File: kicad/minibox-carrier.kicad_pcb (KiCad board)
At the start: 2 copper layers, 109 x 101 mm, 9 parts, among them J1 ESP32-S3 LEFT - USB AT BOTTOM, J10 LCD VCC - WIRE AFTER VOLTAGE 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, J2 ESP32-S3 RIGHT - USB AT BOTTOM, J3 INMP441 VDD GND SCK WS SD L/R, J4 MAX98357A LRC BCLK DIN GAIN S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, J5 PCF8563T CLK INT SDA SCL VCC 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, J6 ST7796 PROVISIONAL HEADER, J7 SWITCH IN LOAD GND - VERIFY O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, J8 EXTERNAL 5V INPUT + GND

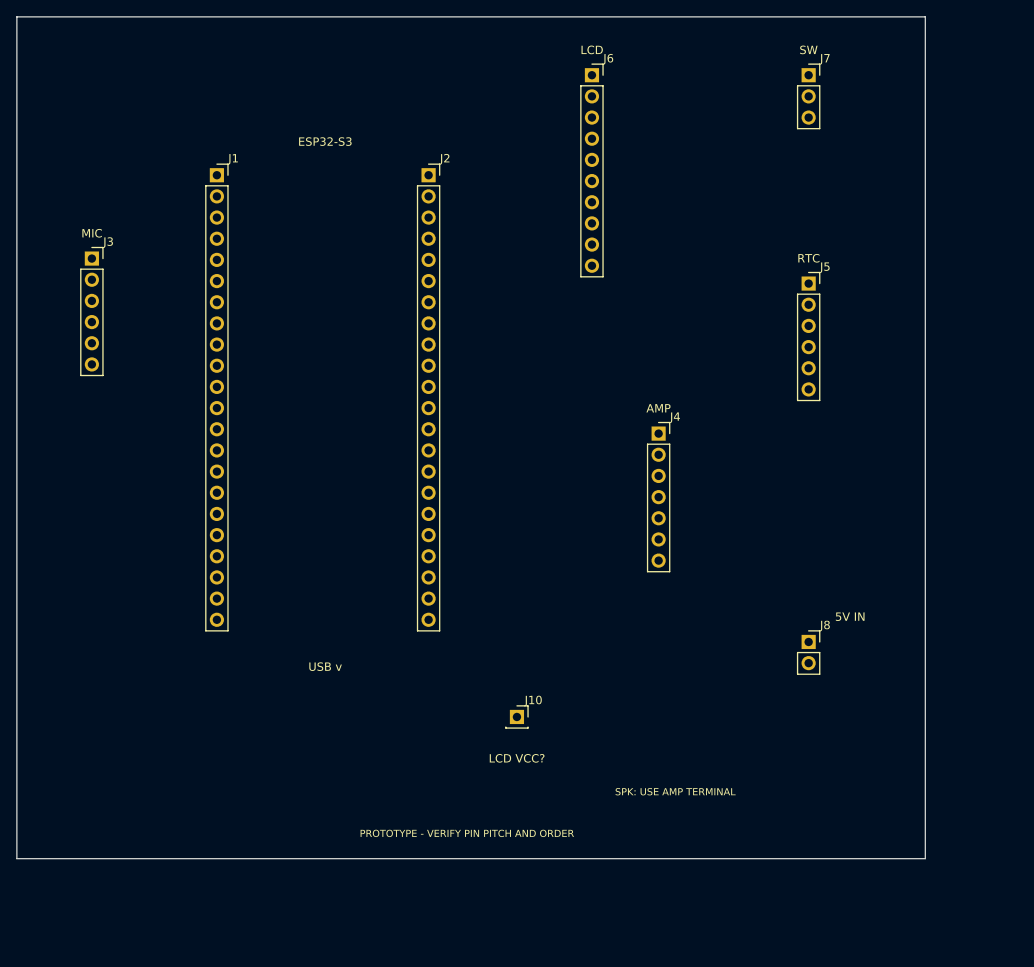
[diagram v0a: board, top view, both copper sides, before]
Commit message: Route Minibox carrier and document module pinouts
Co-authored-by: Copilot App <223556219+Copilot@users.noreply.github.com>
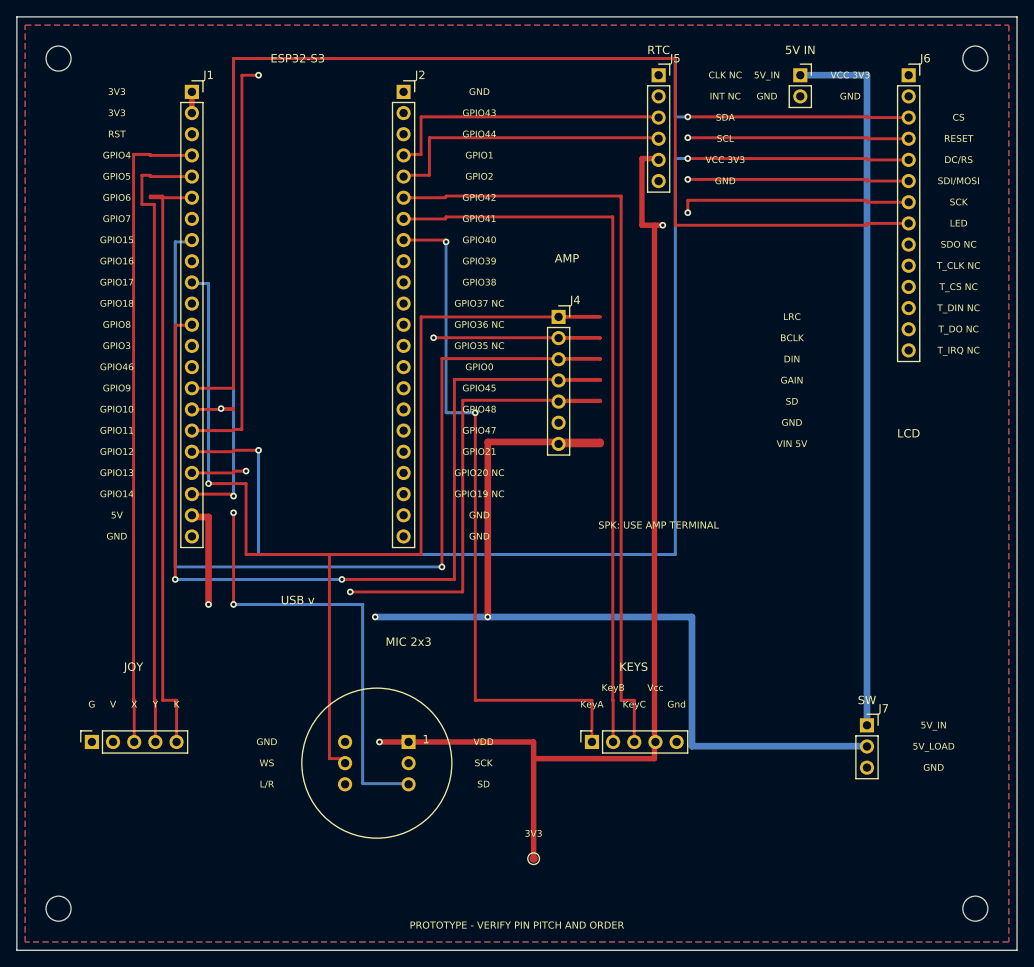
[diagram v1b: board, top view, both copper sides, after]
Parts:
- removed J10: LCD VCC - WIRE AFTER VOLTAGE CHECK, Connector_PinSocket_2.54mm:PinSocket_1x01_P2.54mm_Vertical
- added H1: MountingHole_3mm, MountingHole:MountingHole_3mm, F.Cu at (8.00, 8.00)
- added H2: MountingHole_3mm, MountingHole:MountingHole_3mm, F.Cu at (118.0, 8.00)
- added H3: MountingHole_3mm, MountingHole:MountingHole_3mm, F.Cu at (8.00, 110.0)
- added H4: MountingHole_3mm, MountingHole:MountingHole_3mm, F.Cu at (118.0, 110.0)
- added J11: THREE-KEY CABLE KeyA KeyB KeyC Vcc Gnd, Connector_PinSocket_2.54mm:PinSocket_1x05_P2.54mm_Vertical, F.Cu at (72.0, 90.0)
- added J12: JOYSTICK CABLE G V X Y K, Connector_PinSocket_2.54mm:PinSocket_1x05_P2.54mm_Vertical, F.Cu at (12.0, 90.0)
- added TP1: 3V3, TestPoint:TestPoint_Pad_D1.0mm, F.Cu at (65.0, 104.0)
- J3: value INMP441 VDD GND SCK WS SD L/R -> INMP441 2x3 VDD GND / SCK WS / SD LR; footprint Connector_PinSocket_2.54mm:PinSocket_1x06_P2.54mm_Vertical -> Minibox:INMP441_2x03_Row7.62mm
- J6: value ST7796 PROVISIONAL HEADER -> ST7796 14-PIN DISPLAY HEADER; footprint Connector_PinSocket_2.54mm:PinSocket_1x10_P2.54mm_Vertical -> Connector_PinSocket_2.54mm:PinSocket_1x14_P2.54mm_Vertical
- moved J7 78.3 mm to (105.0, 88.0)
- moved J3 69.3 mm to (50.0, 90.0)
- moved J8 68.0 mm to (97.0, 10.0)
- moved J6 38.0 mm to (110.0, 10.0)
- moved J5 30.8 mm to (80.0, 10.0)
- moved J4 18.4 mm to (68.0, 39.0)
- moved J1 10.4 mm to (24.0, 12.0)
- moved J2 10.4 mm to (49.4, 12.0)
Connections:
- J6 pad 1: LCD_VCC -> 3V3
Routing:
- net 3V3: track 0.00 -> 280.9 mm, vias 0 -> 2
- net LCD_SCK: track 0.00 -> 149.3 mm, vias 0 -> 2
- net 5V_SW: track 0.00 -> 148.5 mm, vias 0 -> 3
- net I2S_BCLK: track 0.00 -> 147.3 mm, vias 0 -> 1
- net LCD_DC: track 0.00 -> 146.3 mm, vias 0 -> 2
- net LCD_CS: track 0.00 -> 145.8 mm, vias 0 -> 2
- net LCD_BL: track 0.00 -> 145.8 mm
- net LCD_RST: track 0.00 -> 145.3 mm, vias 0 -> 2
- net LCD_MOSI: track 0.00 -> 145.3 mm, vias 0 -> 2
- net I2S_WS: track 0.00 -> 142.3 mm, vias 0 -> 1
- net AMP_SD: track 0.00 -> 129.4 mm, vias 0 -> 1
- net AUDIO_DIN: track 0.00 -> 122.3 mm, vias 0 -> 1
- net AMP_GAIN: track 0.00 -> 112.7 mm, vias 0 -> 2
- net BUTTON3: track 0.00 -> 93.3 mm
- net RECORD: track 0.00 -> 88.3 mm
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- added copper zone on B.Cu, net GND
- added copper zone on F.Cu, net GND
- added copper zone on In1.Cu, net GND
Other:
- board size 109 x 101 mm -> 120 x 112 mm
- copper layers 2 -> 4
- board text added: "3V3"
- board text added: "5V"
- board text added: "5V_IN"
- board text added: "5V_LOAD"
- board text added: "BCLK"
- board text added: "CLK NC"
- board text added: "CS"
- board text added: "DC/RS"
- board text added: "DIN"
- board text added: "G"
- board text added: "GAIN"
- board text added: "GND"
- board text added: "GPIO0"
- board text added: "GPIO1"
- board text added: "GPIO10"
- board text added: "GPIO11"
- board text added: "GPIO12"
- board text added: "GPIO13"
- board text added: "GPIO14"
- board text added: "GPIO15"
- board text added: "GPIO16"
- board text added: "GPIO17"
- board text added: "GPIO18"
- board text added: "GPIO19 NC"
- board text added: "GPIO2"
- board text added: "GPIO20 NC"
- board text added: "GPIO21"
- board text added: "GPIO3"
- board text added: "GPIO35 NC"
- board text added: "GPIO36 NC"
- board text added: "GPIO37 NC"
- board text added: "GPIO38"
- board text added: "GPIO39"
- board text added: "GPIO4"
- board text added: "GPIO40"
- board text added: "GPIO41"
- board text added: "GPIO42"
- board text added: "GPIO43"
- board text added: "GPIO44"
- board text added: "GPIO45"
- board text added: "GPIO46"
- board text added: "GPIO47"
- board text added: "GPIO48"
- board text added: "GPIO5"
- board text added: "GPIO6"
- board text added: "GPIO7"
- board text added: "GPIO8"
- board text added: "GPIO9"
- board text added: "Gnd"
- board text added: "INT NC"
- board text added: "JOY"
- board text added: "K"
- board text added: "KEYS"
- board text added: "KeyA"
- board text added: "KeyB"
- board text added: "KeyC"
- board text added: "L/R"
- board text added: "LED"
- board text added: "LRC"
- board text added: "MIC 2x3"
- board text added: "RESET"
- board text added: "RST"
- board text added: "SCK"
- board text added: "SCL"
- board text added: "SD"
- board text added: "SDA"
- board text added: "SDI/MOSI"
- board text added: "SDO NC"
- board text added: "T_CLK NC"
- board text added: "T_CS NC"
- board text added: "T_DIN NC"
- board text added: "T_DO NC"
- board text added: "T_IRQ NC"
- board text added: "V"
- board text added: "VCC 3V3"
- board text added: "VDD"
- board text added: "VIN 5V"
- board text added: "Vcc"
- board text added: "WS"
- board text added: "X"
- board text added: "Y"
- board text removed: "LCD VCC?"
- board text removed: "MIC"

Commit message: Tighten KiCad carrier rules for JLCPCB fabrication
Co-authored-by: Copilot App <223556219+Copilot@users.noreply.github.com>
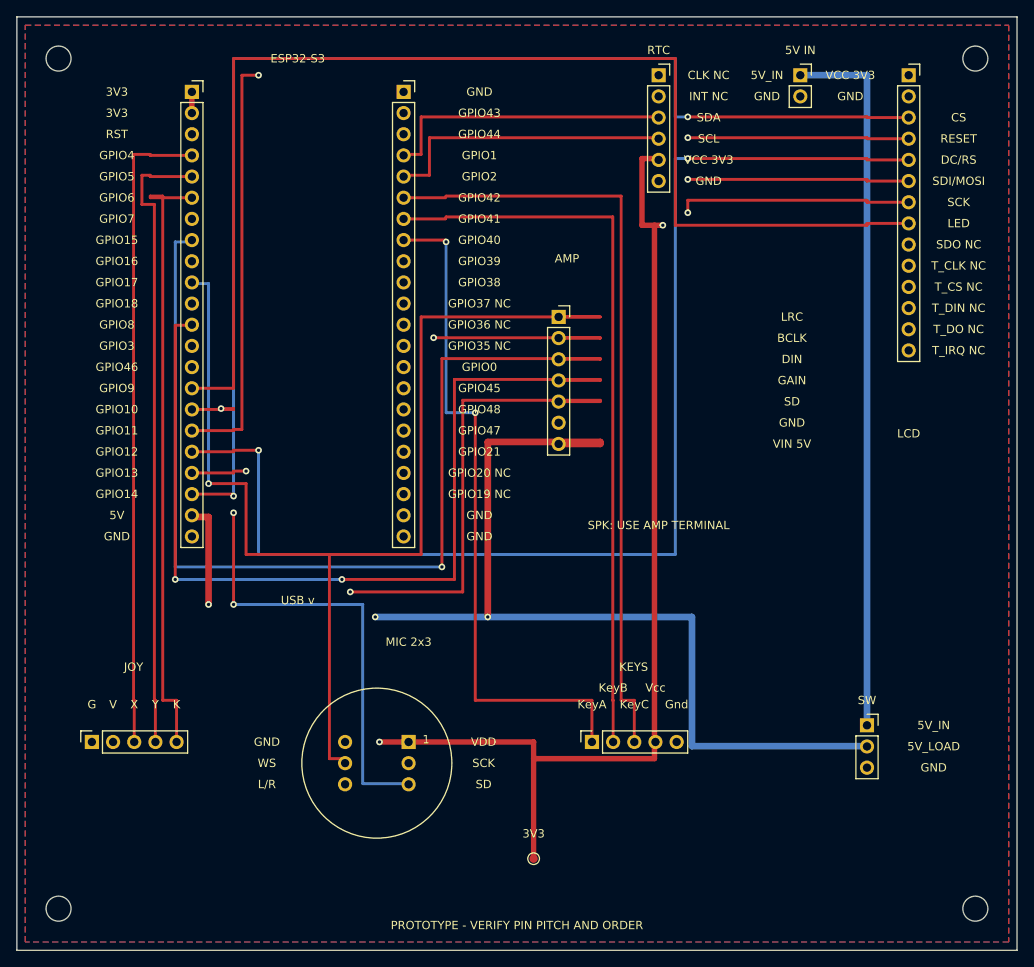
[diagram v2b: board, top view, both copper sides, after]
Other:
- rule pad_to_mask_clearance: 0 -> 0.05

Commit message: Rotate carrier, clear antenna and export JLCPCB Gerbers
Co-authored-by: Copilot App <223556219+Copilot@users.noreply.github.com>
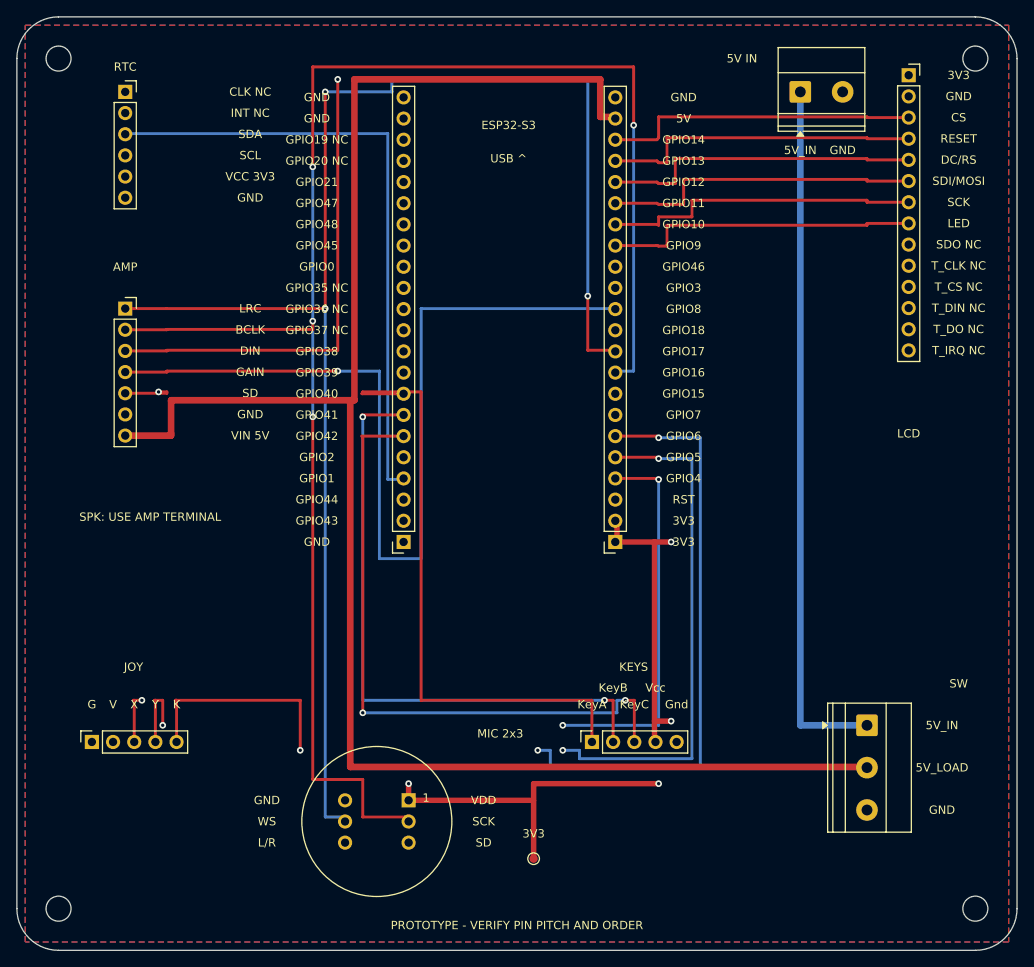
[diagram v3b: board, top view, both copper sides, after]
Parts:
- J1: value ESP32-S3 LEFT - USB AT BOTTOM -> ESP32-S3 LEFT - USB AT TOP
- J2: value ESP32-S3 RIGHT - USB AT BOTTOM -> ESP32-S3 RIGHT - USB AT TOP
- J7: value SWITCH IN LOAD GND - VERIFY ORDER -> 5.08mm wire terminal; footprint Connector_PinSocket_2.54mm:PinSocket_1x03_P2.54mm_Vertical -> TerminalBlock_Phoenix:TerminalBlock_Phoenix_MKDS-1,5-3-5.08_1x03_P5.08mm_Horizontal
- J8: value EXTERNAL 5V INPUT + GND -> 5.08mm wire terminal; footprint Connector_PinSocket_2.54mm:PinSocket_1x02_P2.54mm_Vertical -> TerminalBlock_Phoenix:TerminalBlock_Phoenix_MKDS-1,5-2-5.08_1x02_P5.08mm_Horizontal
- moved J1 74.1 mm to (74.8, 66.0), turned to 180 degrees
- moved J5 64.0 mm to (16.0, 12.0)
- moved J2 54.0 mm to (49.4, 66.0), turned to 180 degrees
- moved J4 52.0 mm to (16.0, 38.0)
- moved J3 7.00 mm to (50.0, 97.0)
- moved J8 2.00 mm to (97.0, 12.0)
- turned J7 to -90 degrees
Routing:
- net LCD_SCK: track 149.3 -> 38.5 mm, vias 2 -> 0
- net LCD_CS: track 145.8 -> 37.9 mm, vias 2 -> 0
- net LCD_DC: track 146.3 -> 38.4 mm, vias 2 -> 0
- net LCD_BL: track 145.8 -> 37.9 mm
- net LCD_RST: track 145.3 -> 38.4 mm, vias 2 -> 0
- net LCD_MOSI: track 145.3 -> 38.4 mm, vias 2 -> 0
- net 5V_SW: track 148.5 -> 212.6 mm, vias 3 -> 0
- net I2S_BCLK: track 147.3 -> 202.8 mm, vias 1 -> 4
- net GPIO6: track 73.9 -> 125.9 mm, vias 0 -> 3
- net GPIO5: track 75.8 -> 121.9 mm, vias 0 -> 3
- net I2S_WS: track 142.3 -> 183.4 mm, vias 1 -> 3
- net RTC_SDA: track 35.2 -> 75.2 mm
- net RTC_SCL: track 35.3 -> 70.3 mm
- net AMP_SD: track 129.4 -> 98.5 mm
- net GPIO4: track 77.7 -> 105.8 mm, vias 0 -> 3
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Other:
- outline, holes or cut-outs redrawn
- board text added: "USB ^"
- board text removed: "USB v"

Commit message: Refine two-layer carrier routing, GPIO silk and solderable pads
Export front and back PNG previews with material legends and refresh two-layer Gerbers.

Co-authored-by: Copilot App <223556219+Copilot@users.noreply.github.com>
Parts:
- removed TP1: 3V3, TestPoint:TestPoint_Pad_D1.0mm
- moved J7 16.0 mm to (105.0, 72.0)
- moved J11 10.2 mm to (82.0, 88.0)
- moved J6 8.00 mm to (110.0, 18.0)
- moved J4 4.00 mm to (12.0, 38.0)
- moved J3 3.00 mm to (50.0, 100.0)
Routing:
- net GND: track 0.00 -> 335.3 mm
- net AMP_SD: track 98.5 -> 170.3 mm, vias 1 -> 2
- net I2S_WS: track 183.4 -> 241.5 mm, vias 3 -> 5
- net I2S_BCLK: track 202.8 -> 259.0 mm, vias 4 -> 5
- net GPIO4: track 105.8 -> 156.8 mm, vias 3 -> 2
- net GPIO6: track 125.9 -> 175.3 mm, vias 3 -> 2
- net LCD_SCK: track 38.5 -> 87.5 mm, vias 0 -> 2
- net GPIO5: track 121.9 -> 164.6 mm, vias 3 -> 2
- net 5V_SW: track 212.6 -> 186.0 mm, vias 0 -> 3
- net MIC_SD: track 91.8 -> 115.1 mm
- net AUDIO_DIN: track 129.4 -> 149.8 mm, vias 1 -> 4
- net 5V_IN: track 84.0 -> 65.7 mm
- net 3V3: track 281.4 -> 296.5 mm, vias 4 -> 10
- net LCD_MOSI: track 38.4 -> 52.4 mm, vias 0 -> 2
- net BUTTON3: track 77.3 -> 88.7 mm
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- removed copper zone on In1.Cu, net GND
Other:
- copper layers 4 -> 2
- board text added: "BCLK GPIO16"
- board text added: "CS GPIO14"
- board text added: "DC/RS GPIO12"
- board text added: "DIN GPIO15"
- board text added: "GAIN GPIO8"
- board text added: "K GPIO6"
- board text added: "KeyA GPIO40"
- board text added: "KeyB GPIO41"
- board text added: "KeyC GPIO42"
- board text added: "L/R GND"
- board text added: "LED GPIO9"
- board text added: "LRC GPIO17"
- board text added: "RESET GPIO13"
- board text added: "SCK GPIO10"
- board text added: "SCK GPIO16"
- board text added: "SCL GPIO2"
- board text added: "SD GPIO18"
- board text added: "SD GPIO7"
- board text added: "SDA GPIO1"
- board text added: "SDI/MOSI GPIO11"
- board text added: "WS GPIO17"
- board text added: "X GPIO4"
- board text added: "Y GPIO5"
- board text removed: "BCLK"
- board text removed: "CS"
- board text removed: "DC/RS"
- board text removed: "DIN"
- board text removed: "GAIN"
- board text removed: "K"
- board text removed: "KeyA"
- board text removed: "KeyB"
- board text removed: "KeyC"
- board text removed: "L/R"
- board text removed: "LED"
- board text removed: "LRC"
- board text removed: "RESET"
- board text removed: "SCK"
- board text removed: "SCL"
- board text removed: "SD"
- board text removed: "SDA"
- board text removed: "SDI/MOSI"
- board text removed: "WS"
- board text removed: "X"
- board text removed: "Y"
